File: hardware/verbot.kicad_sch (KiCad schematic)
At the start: 3 parts, among them J1 Raspberry Pi Zero 2 W, J2 5V USB power bank, M1 Pimoroni OnOff SHIM

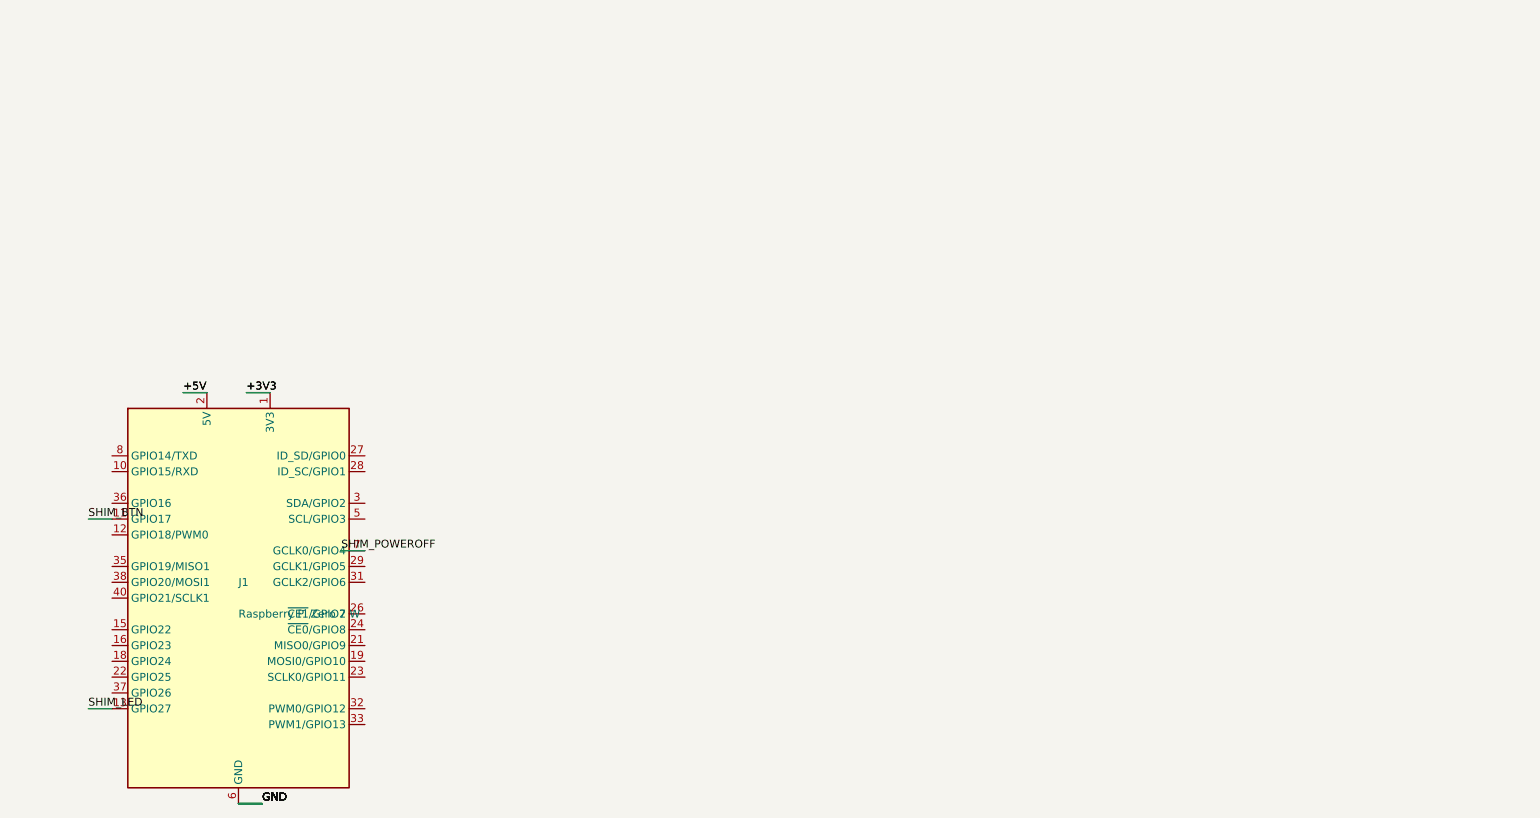
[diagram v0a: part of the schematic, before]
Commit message: feat(hardware): DRV8833 motor section
Wires the DRV8833 carrier to the Pi (IN1/IN2/EEP/ULT on BCM12/13/6/16)
and to the Verbot motor, per src/verbot/config.py and docs/hardware.md.
Channel B is left no-connected. Motor_DC is sourced from the Motor
library rather than Device, where it doesn't exist on this system's
symbol set; its pin numbers match what the plan assumed.
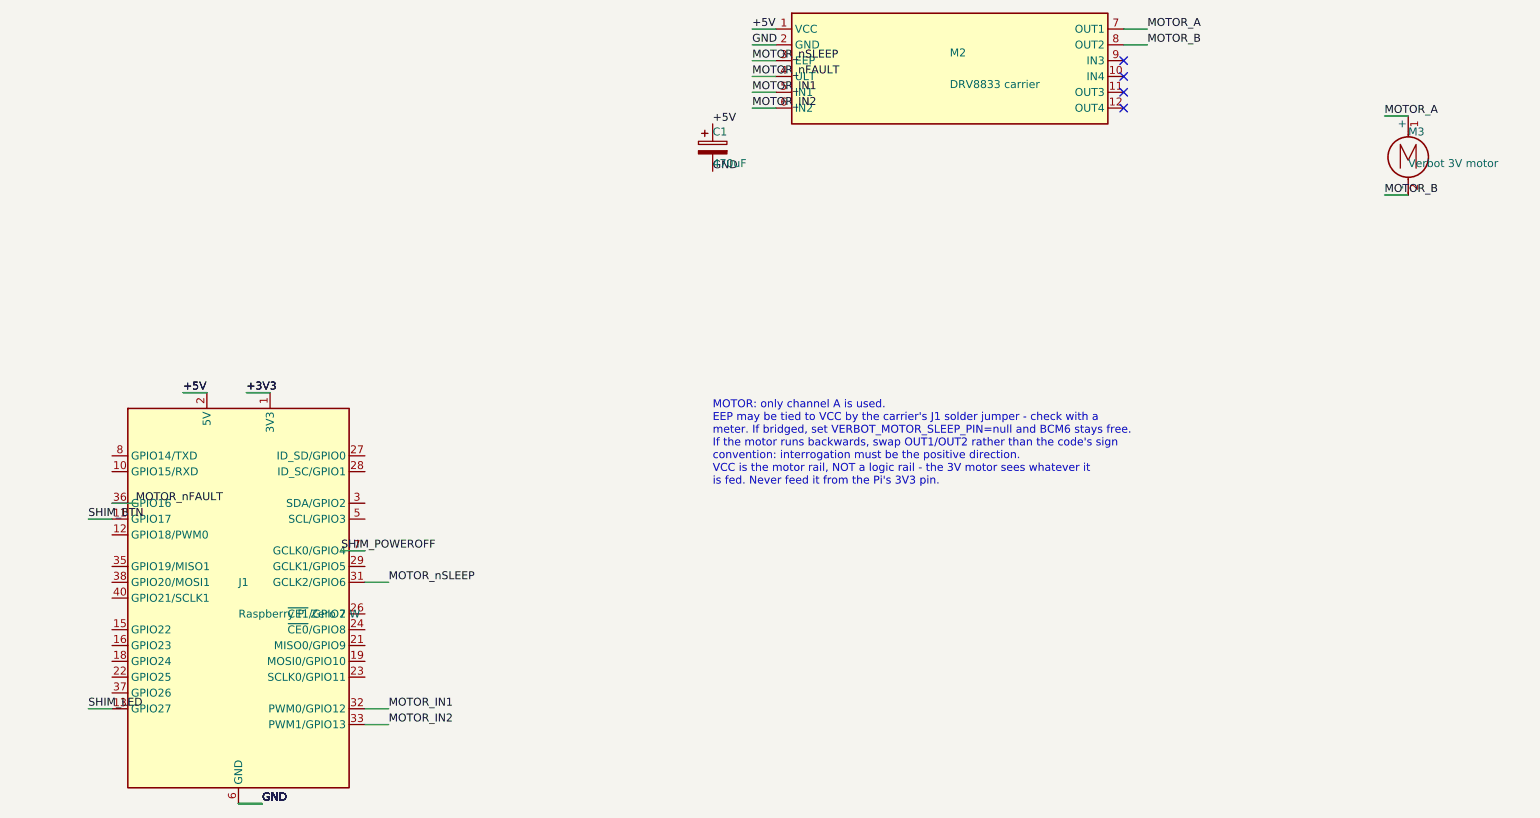
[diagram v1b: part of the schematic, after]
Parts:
- added C1: 470uF, symbol Device:C_Polarized
- added M2: DRV8833 carrier, symbol verbot:DRV8833_Carrier
- added M3: Verbot 3V motor, symbol Motor:Motor_DC
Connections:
- net +5V: now also C1.1, M2.1 (VCC)
- net GND: now also C1.2, M2.2 (GND)
- net MOTOR_nSLEEP: now reaches J1.31 (GCLK2/GPIO6)
- net MOTOR_nSLEEP: now also M2.3 (EEP)
- net MOTOR_IN1: now reaches J1.32 (PWM0/GPIO12)
- net MOTOR_IN1: now also M2.5 (IN1)
- net MOTOR_IN2: now reaches J1.33 (PWM1/GPIO13)
- net MOTOR_IN2: now also M2.6 (IN2)
- net MOTOR_nFAULT: now reaches J1.36 (GPIO16)
- net MOTOR_nFAULT: now also M2.4 (ULT)
- new net MOTOR_A: M2.7 (OUT1), M3.1 (+)
- new net MOTOR_B: M2.8 (OUT2), M3.2 (-)
- no-connect marks 4 -> 8
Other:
- note added: "MOTOR: only channel A is used. EEP may be tied to VCC by the carrier's J1 solder jumper - check with a meter. If bridged, set VERBOT_MOTOR_SLEEP_PIN=null and BCM6 stays free. If the motor runs backwards, swap OUT1/OUT2 rather than the code's sign convention: interrogation must be the positive direction. VCC is the motor rail, NOT a logic rail - the 3V motor sees whatever it is fed. Never feed it 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"
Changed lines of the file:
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@@
 		(instances
 			(project "verbot"
-				(path "/630b9879-9130-473a-826e-fed863ad0612" (reference "J1") (unit 1))))
+				(path "/607dc9e4-d310-4b00-b4a4-3bee0643b6b6" (reference "J1") (unit 1))))
 	)
 	(symbol
@@
 		(instances
 			(project "verbot"
-				(path "/630b9879-9130-473a-826e-fed863ad0612" (reference "M1") (unit 1))))
+				(path "/607dc9e4-d310-4b00-b4a4-3bee0643b6b6" (reference "M1") (unit 1))))
 	)
 	(symbol
@@
 		(instances
 			(project "verbot"
-				(path "/630b9879-9130-473a-826e-fed863ad0612" (reference "J2") (unit 1))))
+				(path "/607dc9e4-d310-4b00-b4a4-3bee0643b6b6" (reference "J2") (unit 1))))
 	)
 	(wire (pts (xy 26.67 58.42) (xy 30.48 58.42))
@@
 		(instances
 			(project "verbot"
-				(path "/630b9879-9130-473a-826e-fed863ad0612" (reference "#FLG01") (unit 1))))
+				(path "/607dc9e4-d310-4b00-b4a4-3bee0643b6b6" (reference "#FLG01") (unit 1))))
 	)
 	(label "+5V" (at 44.45 105.41 0)
@@
 		(instances
 			(project "verbot"
-				(path "/630b9879-9130-473a-826e-fed863ad0612" (reference "#FLG02") (unit 1))))
+				(path "/607dc9e4-d310-4b00-b4a4-3bee0643b6b6" (reference "#FLG02") (unit 1))))
 	)
 	(label "+3V3" (at 69.85 105.41 0)
@@
 	(text "POWER: 5V USB bank -> OnOff SHIM -> Pi 5V rail and DRV8833 VCC.\nMotor current therefore passes through the SHIM load switch (~2A).\nCap VERBOT_ACTION_SPEED near +/-60 and rely on C1 for transients." (at 25.4 120.65 0)
 		(effects (font (size 1.27 1.27)) (justify left top)))
+	(symbol
+		(lib_id "verbot:DRV8833_Carrier")
+		(at 330.2 63.5 0)
+		(unit 1)
+		(exclude_from_sim no)
+		(in_bom yes)
+		(on_board yes)
+		(dnp no)
+		(property "Reference" "M2" (at 330.2 60.96 0)
+			(effects (font (size 1.27 1.27)) (justify left)))
+		(property "Value" "DRV8833 carrier" (at 330.2 66.04 0)
+			(effects (font (size 1.27 1.27)) (justify left) ))
+		(pin "1")
+		(pin "2")
+		(pin "3")
+		(pin "4")
+		(pin "5")
+		(pin "6")
+		(pin "7")
+		(pin "8")
+		(pin "9")
+		(pin "10")
+		(pin "11")
+		(pin "12")
+		(instances
+			(project "verbot"
+				(path "/607dc9e4-d310-4b00-b4a4-3bee0643b6b6" (reference "M2") (unit 1))))
+	)
+	(symbol
+		(lib_id "Motor:Motor_DC")
+		(at 403.86 76.2 0)
+		(unit 1)
+		(exclude_from_sim no)
+		(in_bom yes)
+		(on_board yes)
+		(dnp no)
+		(property "Reference" "M3" (at 403.86 73.66 0)
+			(effects (font (size 1.27 1.27)) (justify left)))
+		(property "Value" "Verbot 3V motor" (at 403.86 78.74000000000001 0)
+			(effects (font (size 1.27 1.27)) (justify left) ))
+		(pin "1")
+		(pin "2")
+		(instances
+			(project "verbot"
+				(path "/607dc9e4-d310-4b00-b4a4-3bee0643b6b6" (reference "M3") (unit 1))))
+	)
+	(symbol
+		(lib_id "Device:C_Polarized")
+		(at 292.1 76.2 0)
+		(unit 1)
+		(exclude_from_sim no)
+		(in_bom yes)
+		(on_board yes)
+		(dnp no)
+		(property "Reference" "C1" (at 292.1 73.66 0)
+			(effects (font (size 1.27 1.27)) (justify left)))
+		(property "Value" "470uF" (at 292.1 78.74000000000001 0)
+			(effects (font (size 1.27 1.27)) (justify left) ))
+		(pin "1")
+		(pin "2")
+		(instances
+			(project "verbot"
+				(path "/607dc9e4-d310-4b00-b4a4-3bee0643b6b6" (reference "C1") (unit 1))))
+	)
+	(wire (pts (xy 236.22 166.37) (xy 240.03 166.37))
+		(stroke (width 0) (type default)))
+	(label "MOTOR_IN1" (at 240.03 166.37 0)
+		(effects (font (size 1.27 1.27)) (justify left bottom)))
+	(wire (pts (xy 302.26 67.31) (xy 298.45 67.31))
+		(stroke (width 0) (type default)))
+	(label "MOTOR_IN1" (at 298.45 67.31 0)
+		(effects (font (size 1.27 1.27)) (justify left bottom)))
+	(wire (pts (xy 236.22 168.91) (xy 240.03 168.91))
+		(stroke (width 0) (type default)))
+	(label "MOTOR_IN2" (at 240.03 168.91 0)
+		(effects (font (size 1.27 1.27)) (justify left bottom)))
+	(wire (pts (xy 302.26 69.85) (xy 298.45 69.85))
+		(stroke (width 0) (type default)))
+	(label "MOTOR_IN2" (at 298.45 69.85 0)
+		(effects (font (size 1.27 1.27)) (justify left bottom)))
+	(wire (pts (xy 236.22 146.05) (xy 240.03 146.05))
+		(stroke (width 0) (type default)))
+	(label "MOTOR_nSLEEP" (at 240.03 146.05 0)
+		(effects (font (size 1.27 1.27)) (justify left bottom)))
+	(wire (pts (xy 302.26 62.23) (xy 298.45 62.23))
+		(stroke (width 0) (type default)))
+	(label "MOTOR_nSLEEP" (at 298.45 62.23 0)
+		(effects (font (size 1.27 1.27)) (justify left bottom)))
+	(wire (pts (xy 195.58 133.35) (xy 199.39 133.35))
+		(stroke (width 0) (type default)))
+	(label "MOTOR_nFAULT" (at 199.39 133.35 0)
+		(effects (font (size 1.27 1.27)) (justify left bottom)))
+	(wire (pts (xy 302.26 64.77) (xy 298.45 64.77))
+		(stroke (width 0) (type default)))
+	(label "MOTOR_nFAULT" (at 298.45 64.77 0)
+		(effects (font (size 1.27 1.27)) (justify left bottom)))
+	(wire (pts (xy 302.26 57.15) (xy 298.45 57.15))
+		(stroke (width 0) (type default)))
+	(label "+5V" (at 298.45 57.15 0)
+		(effects (font (size 1.27 1.27)) (justify left bottom)))
+	(wire (pts (xy 302.26 59.69) (xy 298.45 59.69))
+		(stroke (width 0) (type default)))
+	(label "GND" (at 298.45 59.69 0)
+		(effects (font (size 1.27 1.27)) (justify left bottom)))
+	(label "+5V" (at 292.1 72.39 0)
+		(effects (font (size 1.27 1.27)) (justify left bottom)))
+	(label "GND" (at 292.1 80.01 0)
+		(effects (font (size 1.27 1.27)) (justify left bottom)))
+	(wire (pts (xy 358.14 57.15) (xy 361.95 57.15))
+		(stroke (width 0) (type default)))
+	(label "MOTOR_A" (at 361.95 57.15 0)
+		(effects (font (size 1.27 1.27)) (justify left bottom)))
+	(wire (pts (xy 358.14 59.69) (xy 361.95 59.69))
+		(stroke (width 0) (type default)))
+	(label "MOTOR_B" (at 361.95 59.69 0)
+		(effects (font (size 1.27 1.27)) (justify left bottom)))
+	(wire (pts (xy 403.86 71.12) (xy 400.05 71.12))
+		(stroke (width 0) (type default)))
+	(label "MOTOR_A" (at 400.05 71.12 0)
+		(effects (font (size 1.27 1.27)) (justify left bottom)))
+	(wire (pts (xy 403.86 83.82) (xy 400.05 83.82))
+		(stroke (width 0) (type default)))
+	(label "MOTOR_B" (at 400.05 83.82 0)
+		(effects (font (size 1.27 1.27)) (justify left bottom)))
+	(no_connect (at 358.14 62.23))
+	(no_connect (at 358.14 64.77))
+	(no_connect (at 358.14 67.31))
+	(no_connect (at 358.14 69.85))
+	(text "MOTOR: only channel A is used.\nEEP may be tied to VCC by the carrier's J1 solder jumper - check with a\nmeter. If bridged, set VERBOT_MOTOR_SLEEP_PIN=null and BCM6 stays free.\nIf the motor runs backwards, swap OUT1/OUT2 rather than the code's sign\nconvention: interrogation must be the positive direction.\nVCC is the motor rail, NOT a logic rail - the 3V motor sees whatever it\nis fed. Never feed it from the Pi's 3V3 pin." (at 292.1 116.84 0)
+		(effects (font (size 1.27 1.27)) (justify left top)))
 	(sheet_instances
